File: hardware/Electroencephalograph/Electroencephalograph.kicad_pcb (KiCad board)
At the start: 2 copper layers, 90 x 85 mm, 282 parts, among them J1 Conn_01x08_Male, J2 Conn_01x08_Male, J3 Conn_01x04_Female, J4 Conn_01x04_Female, U1 ADS1298IPAG, U10 TPS60403, U2 OPA330xxD, U3 STM32F030K6Tx, U4 THI3-0511, U5 ADUM2401BRWZ, U7 LP5912-1.8DRVT, U8 LP5912-1.8DRVT, U9 LP5912-1.8DRVT, Y1 20MHz

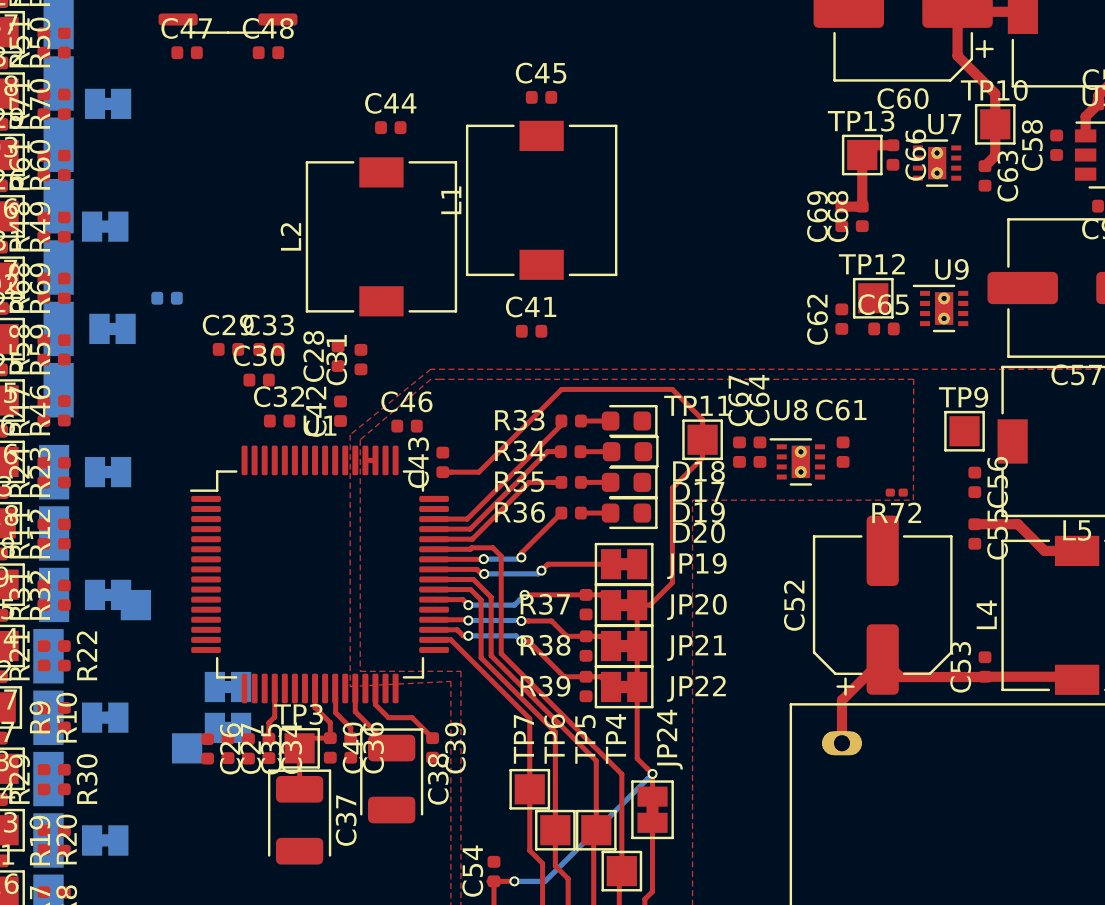
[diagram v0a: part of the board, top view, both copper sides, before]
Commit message: fixes in filtering caps placing
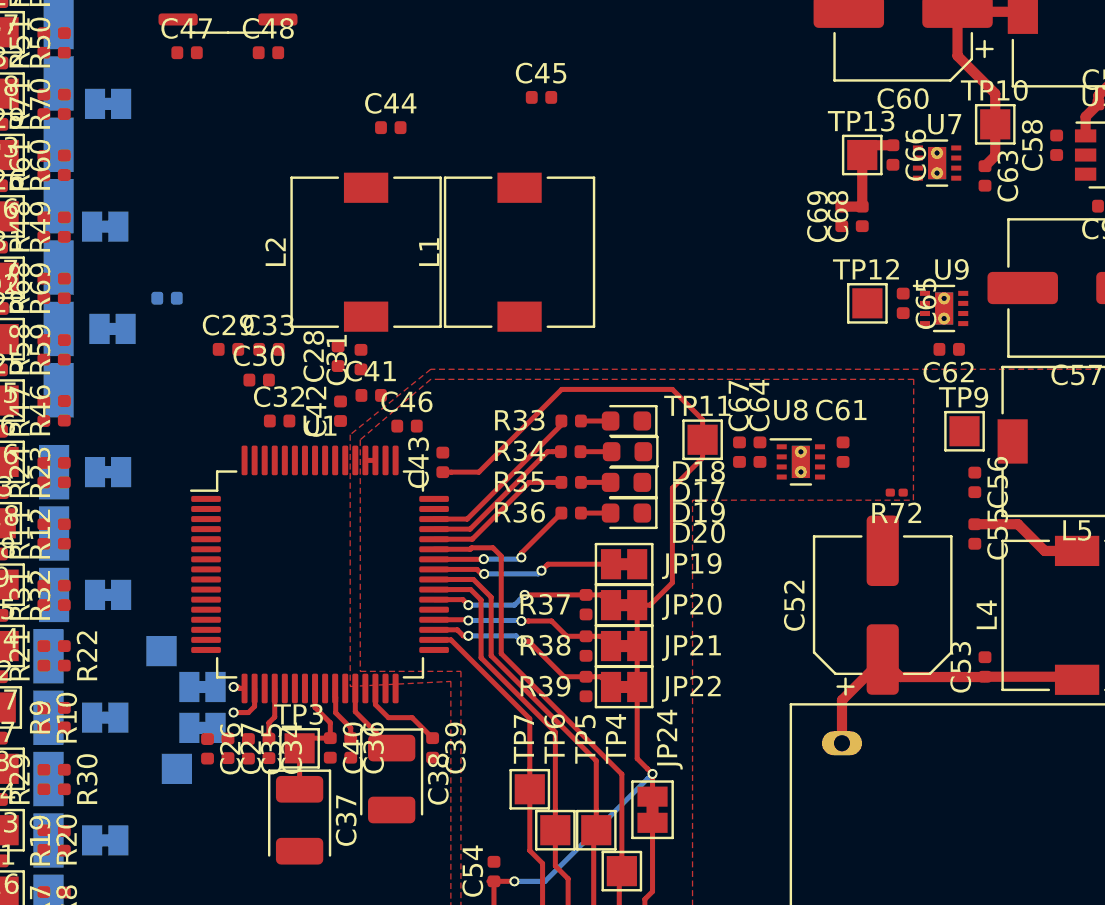
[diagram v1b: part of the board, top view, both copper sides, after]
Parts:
- moved C41 8.58 mm to (98.0, 34.8)
- moved C62 5.54 mm to (126.7, 32.5), turned to 180 degrees
- moved L1 2.80 mm to (105.4, 27.7)
- moved TP1 2.62 mm to (87.6, 47.5)
- moved C65 1.59 mm to (124.5, 30.2), turned to 270 degrees
- moved JP17 1.27 mm to (89.7, 49.3)
- moved JP18 1.27 mm to (89.7, 51.3)
- moved TP2 1.14 mm to (88.4, 53.3)
- moved L2 1.08 mm to (97.8, 27.7)
- moved TP12 0.39 mm to (122.7, 30.2)
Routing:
- net Net-(JP18-Pad2): track 0.00 -> 2.06 mm, vias 0 -> 1
- net Net-(JP17-Pad2): track 0.00 -> 0.58 mm, vias 0 -> 1

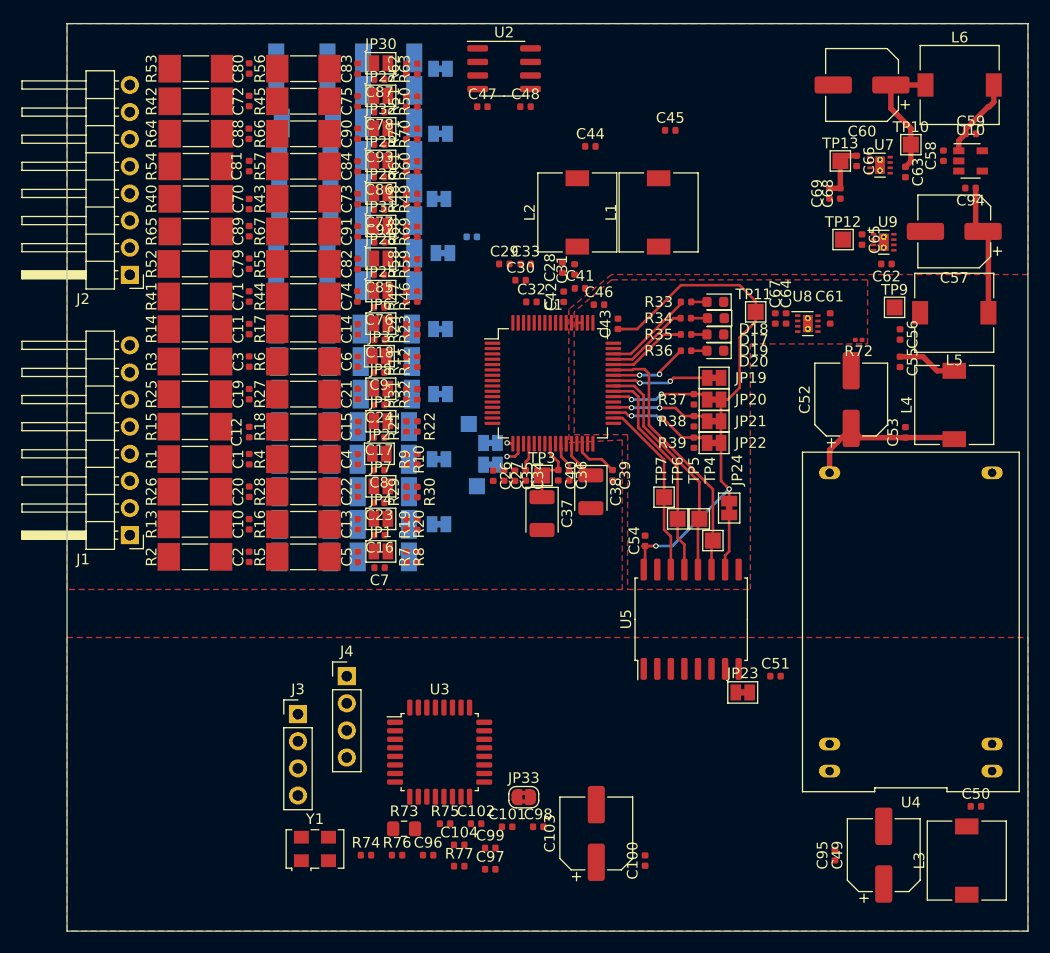
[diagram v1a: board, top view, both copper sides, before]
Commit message: routing of analog power supply
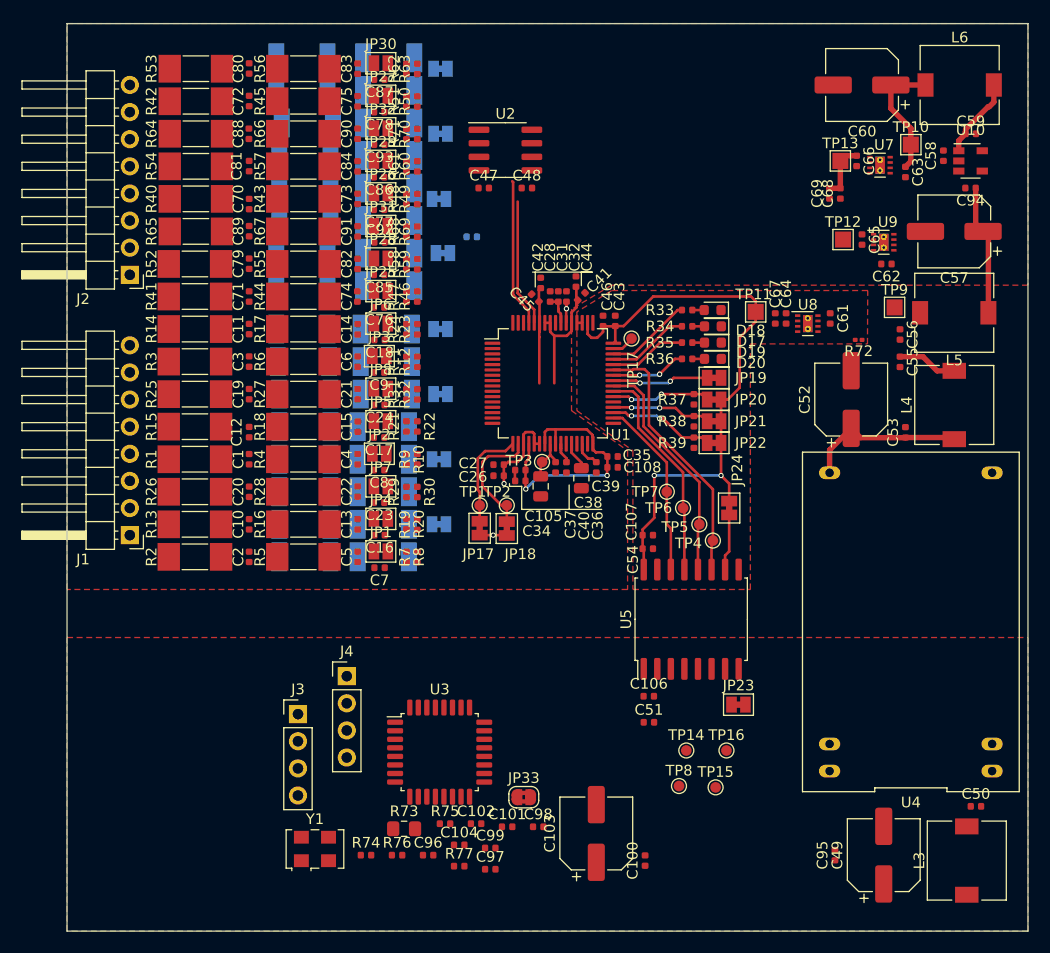
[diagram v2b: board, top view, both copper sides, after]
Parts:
- removed C29, C33: 1u, Capacitor_SMD:C_0402_1005Metric
- removed C30: 100n, Capacitor_SMD:C_0402_1005Metric
- removed L1, L2: 22u, Electroencephalograph:L_7.3x7.3_H3.5
- added C105: 2u2, Capacitor_SMD:C_0402_1005Metric, F.Cu at (92.5, 51.8)
- added C106: 100n, Capacitor_SMD:C_0402_1005Metric, F.Cu at (104.5, 73.0)
- added C107: 100n, Capacitor_SMD:C_0402_1005Metric, F.Cu at (104.4, 57.9)
- added C108: 2u2, Capacitor_SMD:C_0402_1005Metric, F.Cu at (101.1, 51.6)
- added TP14: TestPoint, TestPoint:TestPoint_Pad_D1.0mm, F.Cu at (108.0, 78.1)
- added TP15: TestPoint, TestPoint:TestPoint_Pad_D1.0mm, F.Cu at (110.7, 81.5)
- added TP16: TestPoint, TestPoint:TestPoint_Pad_D1.0mm, F.Cu at (111.8, 78.1)
- added TP17: TestPoint, TestPoint:TestPoint_Pad_D1.0mm, F.Cu at (102.9, 39.5)
- added TP8: TestPoint, TestPoint:TestPoint_Pad_D1.0mm, F.Cu at (107.3, 81.4)
- C35: value 2u2 -> 100n
- C37, C38: footprint Capacitor_Tantalum_SMD:CP_EIA-3528-21_Kemet-B -> Capacitor_SMD:C_0805_2012Metric
- JP17, JP18: moved to F.Cu
- TP1, TP2: footprint TestPoint:TestPoint_Pad_1.5x1.5mm -> TestPoint:TestPoint_Pad_D1.0mm; moved to F.Cu
- TP3, TP4, TP5, TP6, TP7: footprint TestPoint:TestPoint_Pad_1.5x1.5mm -> TestPoint:TestPoint_Pad_D1.0mm
- moved C45 20.2 mm to (93.9, 35.7), turned to 135 degrees
- moved C44 12.7 mm to (97.7, 34.2), turned to 270 degrees
- moved C51 12.6 mm to (104.5, 75.4)
- moved C35 9.32 mm to (101.1, 50.5), turned to 0 degrees
- moved JP17 8.05 mm to (88.6, 57.3), turned to 90 degrees
- moved TP1 7.69 mm to (88.6, 55.1), turned to 270 degrees
- moved U2 7.62 mm to (91.1, 21.8)
- moved C47 7.62 mm to (89.0, 25.4)
- moved C48 7.62 mm to (93.1, 25.4)
- moved JP18 6.18 mm to (91.2, 57.3), turned to 90 degrees
- moved C32 3.32 mm to (96.8, 35.6), turned to 270 degrees
- moved TP2 3.31 mm to (91.2, 55.1), turned to 270 degrees
- moved C31 2.96 mm to (96.0, 35.6)
- moved C28 2.94 mm to (95.2, 35.6)
- moved C37 2.56 mm to (94.4, 53.3)
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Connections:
- C26 pad 1: A_VDD -> A_GND
- C26 pad 2: A_GND -> A_VDD
- C41 pad 2: Net-(C41-Pad2) -> A_VSS
- C42 pad 1: Net-(C42-Pad1) -> A_VDD
- U1 pad 47: (no net) -> Net-(TP17-Pad1)
- U1 pad 53: Net-(C41-Pad2) -> A_VSS
- U1 pad 54: Net-(C42-Pad1) -> A_VDD
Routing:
- net A_VSS: track 7.91 -> 42.6 mm, vias 0 -> 2
- net A_VDD: track 0.00 -> 22.0 mm, vias 0 -> 3
- net /EEGAcquisition/OPAMP_MAYBE: track 0.00 -> 13.9 mm
- net (no net): track 0.00 -> 12.0 mm
- net Net-(JP18-Pad2): track 2.06 -> 11.4 mm, vias 1 -> 0
- net Net-(JP17-Pad2): track 0.58 -> 9.81 mm, vias 1 -> 0
- net D_VDD: track 48.8 -> 57.3 mm
- net Net-(C28-Pad1): track 0.00 -> 2.57 mm
- net Net-(C37-Pad1): track 6.55 -> 4.29 mm
- net Net-(TP17-Pad1): track 0.00 -> 2.14 mm
- net Net-(C39-Pad1): track 4.33 -> 2.52 mm
- net Net-(C38-Pad1): track 3.71 -> 2.67 mm
- net A_GND: track 0.00 -> 0.91 mm
- net EEG_MISO: track 23.8 -> 24.4 mm

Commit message: route of analog part, update of 3d render
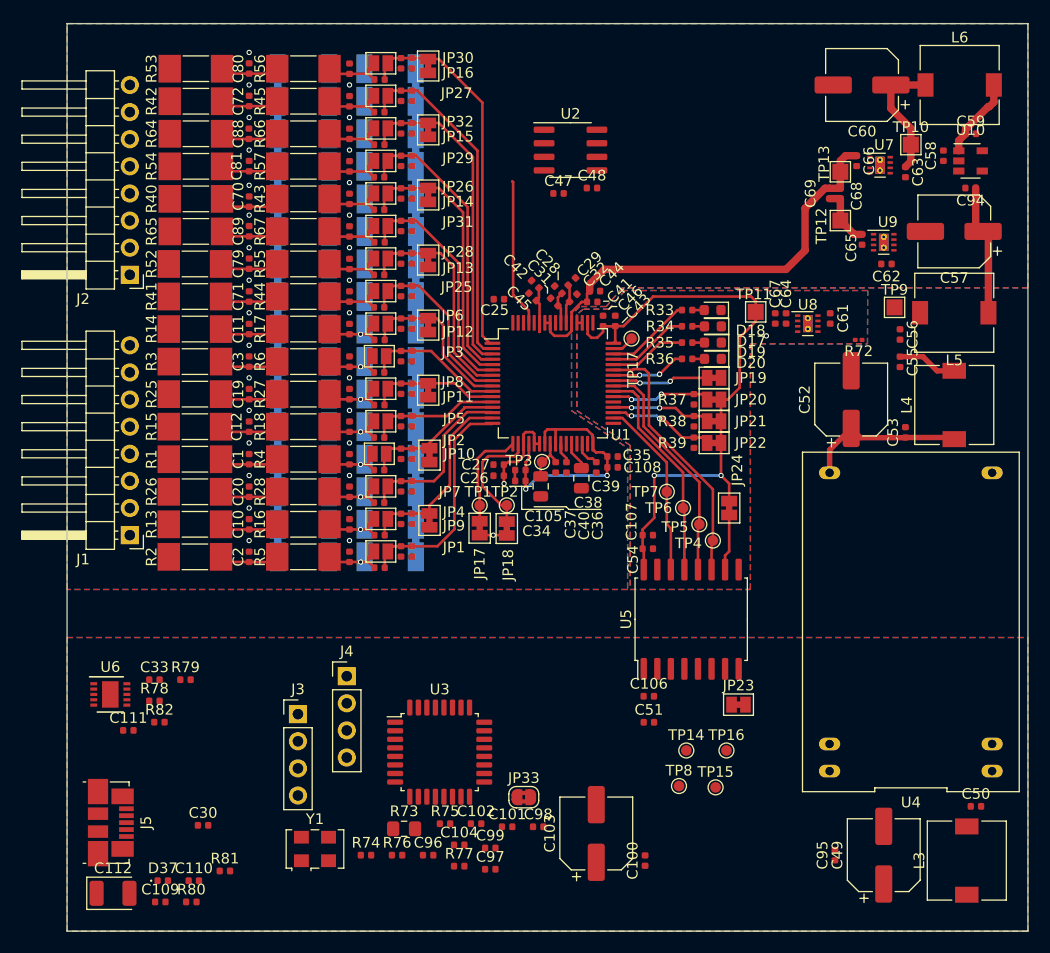
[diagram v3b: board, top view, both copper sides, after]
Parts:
- added C109: 100n, Capacitor_SMD:C_0402_1005Metric, F.Cu at (58.7, 92.3)
- added C110: 100n, Capacitor_SMD:C_0402_1005Metric, F.Cu at (61.9, 90.3)
- added C111: 100n, Capacitor_SMD:C_0402_1005Metric, F.Cu at (55.7, 76.2)
- added C112: 47u/6V3, Capacitor_Tantalum_SMD:CP_EIA-3528-21_Kemet-B, F.Cu at (54.3, 91.5)
- added C29: 2u2, Capacitor_SMD:C_0402_1005Metric, F.Cu at (97.3, 34.2)
- added C30: 47p, Capacitor_SMD:C_0402_1005Metric, F.Cu at (62.7, 85.1)
- added C33: 47p, Capacitor_SMD:C_0402_1005Metric, F.Cu at (58.2, 71.5)
- added D37: LED, LED_SMD:LED_0402_1005Metric, F.Cu at (59.0, 90.3)
- added J5: USB_B_Micro, Connector_USB:USB_Micro-B_Molex_47346-0001, F.Cu at (54.1, 84.8)
- added R78: 4k7, Resistor_SMD:R_0402_1005Metric, F.Cu at (58.2, 73.4)
- added R79: 10k, Resistor_SMD:R_0402_1005Metric, F.Cu at (61.1, 71.5)
- added R80: 27R, Resistor_SMD:R_0402_1005Metric, F.Cu at (61.6, 92.3)
- added R81: 27R, Resistor_SMD:R_0402_1005Metric, F.Cu at (64.8, 89.4)
- added R82: 120R, Resistor_SMD:R_0402_1005Metric, F.Cu at (58.7, 75.4)
- added U6: FT200XD, Package_DFN_QFN:DFN-10-1EP_3x3mm_P0.5mm_EP1.55x2.48mm, F.Cu at (54.1, 72.8)
- C25, JP10, JP11, JP12, JP13, JP14, JP15, JP16, JP9: moved to F.Cu
- moved D25 8.32 mm to (80.3, 17.3), turned to 180 degrees
- moved D23 8.07 mm to (80.3, 26.4), turned to 180 degrees
- moved D24 8.05 mm to (72.1, 26.4), turned to 180 degrees
- moved D26 8.05 mm to (72.1, 17.3), turned to 180 degrees
- moved D36 8.05 mm to (72.1, 20.3), turned to 180 degrees
- moved D1 7.99 mm to (80.3, 59.9), turned to 180 degrees
- moved D13 7.99 mm to (80.3, 53.8), turned to 180 degrees
- moved D7 7.99 mm to (80.3, 56.9), turned to 180 degrees
- moved D9 7.99 mm to (80.3, 47.8), turned to 180 degrees
- moved D35 7.81 mm to (80.3, 20.3), turned to 180 degrees
- moved D10 7.48 mm to (72.1, 47.8), turned to 180 degrees
- moved D14 7.48 mm to (72.1, 53.8), turned to 180 degrees
- moved D2 7.48 mm to (72.1, 59.9), turned to 180 degrees
- moved D8 7.48 mm to (72.1, 56.9), turned to 180 degrees
- moved C47 7.03 mm to (96.0, 25.9)
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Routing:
- net A_VSS: track 42.6 -> 113.3 mm
- net A_VDD: track 22.0 -> 67.6 mm, vias 3 -> 2
- net ECC_8N: track 0.00 -> 35.5 mm
- net ECC_8P: track 0.00 -> 32.2 mm
- net ECC_7N: track 0.00 -> 30.9 mm
- net ECC_7P: track 0.00 -> 27.2 mm
- net ECC_6N: track 0.00 -> 26.0 mm
- net ECC_6P: track 0.00 -> 22.2 mm
- net ECC_1P: track 0.00 -> 21.3 mm
- net ECC_5N: track 0.00 -> 21.1 mm
- net ECC_1N: track 0.00 -> 18.4 mm
- net ECC_5P: track 0.00 -> 17.4 mm
- net ECC_2P: track 0.00 -> 16.3 mm
- net ECC_4N: track 0.00 -> 15.9 mm
- net ECC_2N: track 0.00 -> 13.7 mm
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- added copper zone on B.Cu, net A_GND
- added copper zone on B.Cu, net DP_GND
- added copper zone on B.Cu, net D_GND
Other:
- net class power_supply added: clearance 0.1778, trace_width 0.7, via_dia 0.5, via_drill 0.3

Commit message: further routing
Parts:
- added D38: D_Schottky, Diode_SMD:D_0805_2012Metric, F.Cu at (124.9, 21.0)
- added D39: D_Schottky, Diode_SMD:D_0805_2012Metric, F.Cu at (125.5, 28.2)
- added U11: GD25D10BOIGR, Package_SO:TSSOP-8_4.4x3mm_P0.65mm, F.Cu at (98.3, 78.5)
- moved J3 49.8 mm to (118.1, 92.5), turned to 270 degrees
- moved J4 29.1 mm to (96.0, 92.5), turned to 90 degrees
- moved U3 22.9 mm to (107.2, 83.3), turned to 135 degrees
- moved C101 13.0 mm to (81.6, 76.6)
- moved C103 13.0 mm to (89.9, 77.2)
- moved C98 13.0 mm to (84.5, 76.6)
- moved JP33 13.0 mm to (83.1, 73.8)
- moved C100 11.7 mm to (106.7, 77.0), turned to 0 degrees
- moved TP15 9.40 mm to (107.7, 72.6)
- moved TP8 9.16 mm to (110.0, 72.6)
- moved TP16 6.41 mm to (106.7, 74.2)
- moved TP14 4.03 mm to (109.0, 74.2)
- moved C51 2.03 mm to (104.4, 73.4)
- moved JP23 0.73 mm to (112.5, 73.2)
- moved C106 0.62 mm to (104.4, 72.4)
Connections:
- TP14 pad 1: (no net) -> CS
- TP15 pad 1: (no net) -> MOSI
- TP16 pad 1: (no net) -> SCK
- TP8 pad 1: (no net) -> MISO
- U3 pad 11: (no net) -> SCK
- U3 pad 12: (no net) -> MISO
- U3 pad 13: (no net) -> MOSI
- U3 pad 14: (no net) -> CS
- U5 pad 3: (no net) -> SCK
- U5 pad 4: (no net) -> MOSI
- U5 pad 5: (no net) -> CS
- U5 pad 6: (no net) -> MISO
